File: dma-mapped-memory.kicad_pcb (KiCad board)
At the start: 4 copper layers, 99.8 x 99.8 mm, 27 parts, among them J1 Conn_01x02_Male, J2 Conn_01x02_Male, J3 Conn_02x30_Odd_Even, U1 AS6C8008-55, U10 74LS157, U11 74LS157, U12 74LS157, U13 74LS157, U14 74LS157, U15 74LS04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

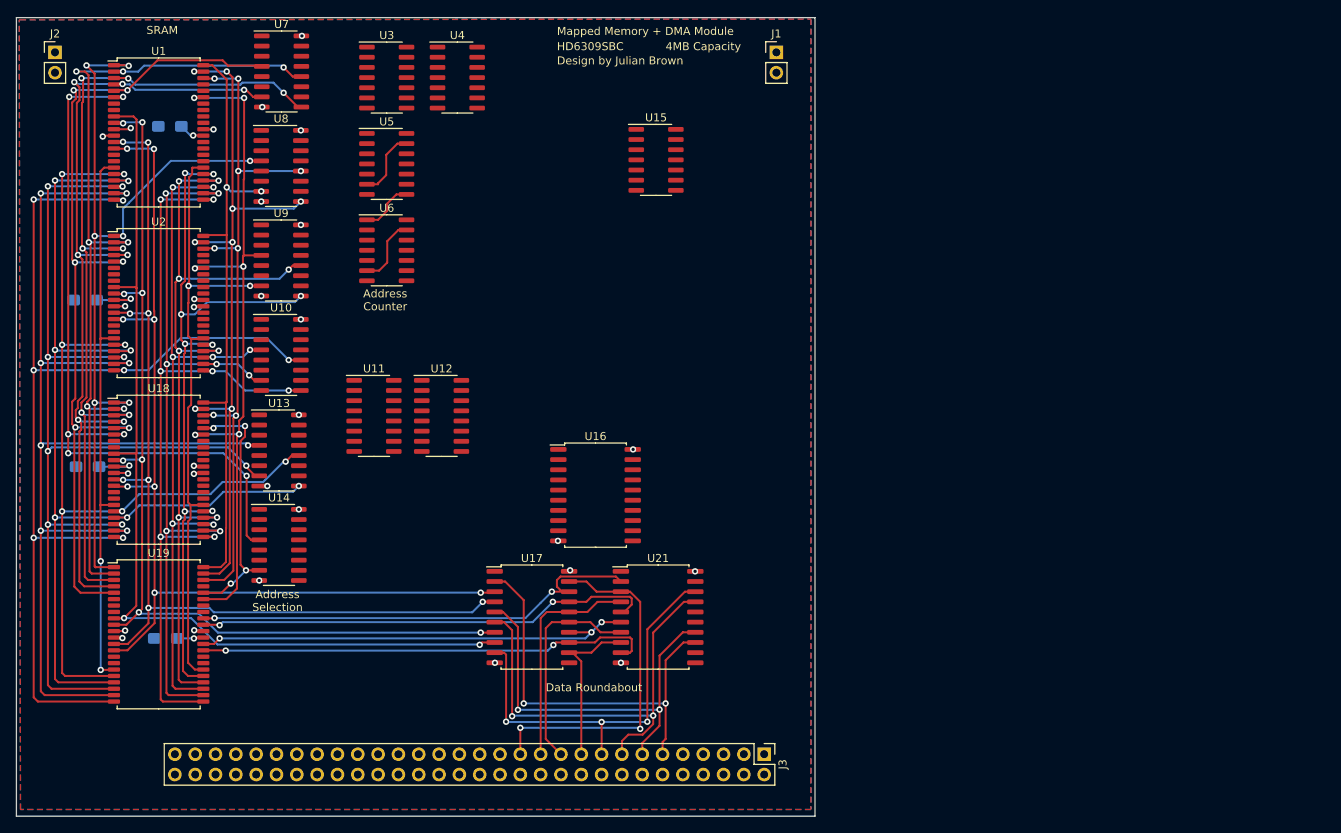
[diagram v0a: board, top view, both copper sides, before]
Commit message: add address registers
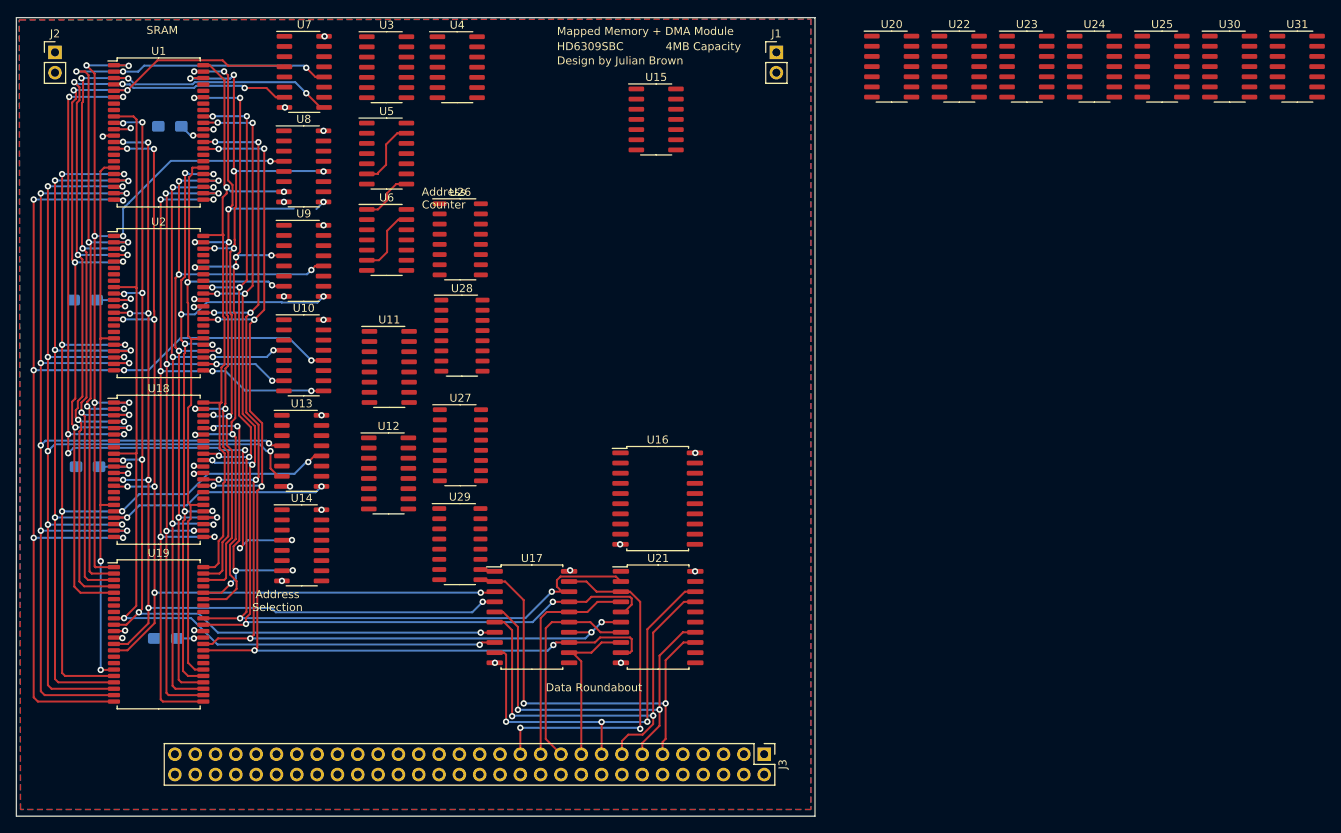
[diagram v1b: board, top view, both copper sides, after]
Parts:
- added U20: 74HC08, Package_SO:SO-14_3.9x8.65mm_P1.27mm, F.Cu at (206.6, 50.3)
- added U22: 74HC21, Package_SO:SO-14_3.9x8.65mm_P1.27mm, F.Cu at (215.0, 50.3)
- added U23: 74HC02, Package_SO:SO-14_3.9x8.65mm_P1.27mm, F.Cu at (223.5, 50.3)
- added U24: 74HC21, Package_SO:SO-14_3.9x8.65mm_P1.27mm, F.Cu at (231.9, 50.3)
- added U25: 74HC04, Package_SO:SO-14_3.9x8.65mm_P1.27mm, F.Cu at (240.4, 50.3)
- added U26: 74HC375, Package_SO:SO-16_3.9x9.9mm_P1.27mm, F.Cu at (152.6, 71.9)
- added U27: 74HC375, Package_SO:SO-16_3.9x9.9mm_P1.27mm, F.Cu at (152.7, 97.6)
- added U28: 74HC375, Package_SO:SO-16_3.9x9.9mm_P1.27mm, F.Cu at (152.8, 83.9)
- added U29: 74HC375, Package_SO:SO-16_3.9x9.9mm_P1.27mm, F.Cu at (152.6, 110.0)
- added U30: 74HC21, Package_SO:SO-14_3.9x8.65mm_P1.27mm, F.Cu at (248.8, 50.3)
- added U31: 74HC04, Package_SO:SO-14_3.9x8.65mm_P1.27mm, F.Cu at (257.3, 50.3)
- moved U12 9.78 mm to (143.7, 101.2)
- moved U16 7.78 mm to (177.3, 104.3)
- moved U11 6.41 mm to (143.8, 87.9)
- moved U15 5.05 mm to (177.1, 56.9)
- moved U10 2.83 mm to (133.1, 86.4)
- moved U7 2.83 mm to (133.1, 51.0)
- moved U8 2.83 mm to (133.1, 62.8)
- moved U13 2.83 mm to (132.8, 98.3)
- moved U14 2.83 mm to (132.8, 110.2)
- moved U9 2.83 mm to (133.1, 74.6)
- moved U3 1.30 mm to (143.4, 50.4)
- moved U4 1.30 mm to (152.3, 50.4)
- moved U5 1.30 mm to (143.4, 61.2)
- moved U6 1.30 mm to (143.4, 72.0)
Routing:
- net DQ4: track 57.2 -> 143.2 mm, vias 2 -> 8
- net DQ5: track 56.2 -> 139.2 mm, vias 3 -> 9
- net DQ6: track 57.7 -> 139.6 mm, vias 2 -> 8
- net DQ7: track 58.2 -> 138.4 mm, vias 2 -> 8
- net DA20: track 94.1 -> 104.4 mm, vias 6 -> 8
- net DA7: track 86.7 -> 92.9 mm
- net DA21: track 32.0 -> 37.2 mm, vias 4 -> 5
- net DA17: track 130.6 -> 135.4 mm
- net DA9: track 78.5 -> 81.9 mm
- net DA3: track 110.1 -> 113.3 mm
- net DA16: track 136.9 -> 140.0 mm
- net DA1: track 108.7 -> 111.8 mm
- net DA0: track 111.3 -> 114.3 mm
- net DA10: track 95.7 -> 98.5 mm
- net DA2: track 112.1 -> 115.0 mm
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
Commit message: simplify logic
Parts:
- removed U25, U31: 74HC04, Package_SO:SO-14_3.9x8.65mm_P1.27mm
- moved U16 11.2 mm to (188.2, 101.4)
- moved U17 11.2 mm to (172.4, 116.2)
- moved U21 11.2 mm to (188.2, 116.2)
- moved U11 4.14 mm to (143.9, 83.7)
- moved U26 3.79 mm to (152.7, 75.7)
- moved U28 3.76 mm to (152.7, 87.7)
- moved U27 1.81 mm to (152.9, 99.5)
- moved U12 1.81 mm to (143.9, 103.0)
- moved U29 1.30 mm to (152.8, 111.3)
- moved U3 0.45 mm to (143.9, 50.3)
- moved U4 0.45 mm to (152.7, 50.3)
- moved U5 0.45 mm to (143.9, 61.1)
- moved U6 0.45 mm to (143.9, 71.9)
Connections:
- U1 pad 40: Net-(U1-CE2) -> ~{DA21}
- U1 pad 41: unconnected-(U1-~{OE}-Pad41) -> E
- U15 pad 10: Net-(U17-OE) -> ~{R}/W
- U15 pad 12: Net-(U21-LE) -> unconnected-(U15-Pad12)
- U15 pad 13: R/~{W} -> unconnected-(U15-Pad13)
- U15 pad 2: Net-(U2-~{CE}) -> ~{DA20}
- U15 pad 3: DA21 -> unconnected-(U15-Pad3)
- U15 pad 4: Net-(U1-CE2) -> unconnected-(U15-Pad4)
- U15 pad 6: Net-(U2-CE2) -> ~{DA21}
- U15 pad 8: Net-(U19-~{CE}) -> unconnected-(U15-Pad8)
- U15 pad 9: DA20 -> unconnected-(U15-Pad9)
- U17 pad 1: Net-(U17-OE) -> ~{R}/W
- U18 pad 41: unconnected-(U18-~{OE}-Pad41) -> E
- U19 pad 41: unconnected-(U19-~{OE}-Pad41) -> E
- U19 pad 6: Net-(U19-~{CE}) -> ~{DA20}
- U2 pad 40: Net-(U2-CE2) -> ~{DA21}
- U2 pad 41: unconnected-(U2-~{OE}-Pad41) -> E
- U2 pad 6: Net-(U2-~{CE}) -> ~{DA20}
- U21 pad 11: Net-(U21-LE) -> ~{R}/W
- U24 pad 9: Net-(U24-Pad9) -> ~{R}/W
- U28 pad 1: D0 -> D1
- U28 pad 3: PBA0 -> PBA1
- U28 pad 5: PBA1 -> PBA0
- U28 pad 7: D1 -> D0
- U29 pad 1: D4 -> D5
- U29 pad 3: PBA4 -> PBA5
- U29 pad 5: PBA5 -> PBA4
- U29 pad 7: D5 -> D4
- U30 pad 9: Net-(U30-Pad9) -> ~{R}/W
- U6 pad 13: Net-(U6A-Q3) -> AM10
- U6 pad 6: Net-(U6A-Q3) -> AM10
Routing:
- net E: track 0.00 -> 267.6 mm, vias 0 -> 9
- net DQ5: track 139.2 -> 95.6 mm
- net D2: track 55.7 -> 12.2 mm, vias 2 -> 0
- net DQ0: track 123.6 -> 82.8 mm, vias 8 -> 7
- net D0: track 51.8 -> 11.3 mm, vias 2 -> 0
- net DQ4: track 143.2 -> 103.7 mm
- net D3: track 51.1 -> 13.5 mm, vias 3 -> 0
- net DQ6: track 139.6 -> 102.7 mm
- net D1: track 50.7 -> 13.8 mm, vias 2 -> 0
- net DQ7: track 138.4 -> 102.2 mm
- net DQ2: track 121.6 -> 88.7 mm
- net DQ3: track 120.8 -> 88.0 mm
- net AM17: track 0.00 -> 31.2 mm, vias 0 -> 2
- net D7: track 44.2 -> 13.2 mm, vias 2 -> 0
- net AM13: track 0.00 -> 28.8 mm, vias 0 -> 4
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
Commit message: continue hand tracing
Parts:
- moved U15 84.7 mm to (132.5, 128.9)
- moved U30 81.1 mm to (178.1, 90.0)
- moved U22 67.7 mm to (169.7, 100.6)
- moved U23 66.9 mm to (169.7, 90.0)
- moved U24 61.3 mm to (178.0, 79.5)
- moved U20 41.5 mm to (169.9, 69.7)
- moved U17 2.19 mm to (174.6, 116.2)
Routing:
- net ~{DA21}: track 0.00 -> 91.1 mm, vias 0 -> 2
- net A0: track 4.94 -> 95.6 mm
- net A3: track 5.35 -> 91.5 mm
- net A1: track 5.13 -> 89.2 mm
- net A2: track 4.79 -> 88.4 mm
- net A5: track 5.21 -> 87.3 mm
- net ~{DA20}: track 0.00 -> 80.2 mm, vias 0 -> 2
- net A4: track 5.29 -> 79.3 mm
- net A7: track 4.66 -> 78.1 mm
- net A11: track 5.22 -> 78.3 mm, vias 0 -> 2
- net A12: track 5.21 -> 76.6 mm, vias 0 -> 2
- net A8: track 5.33 -> 74.5 mm, vias 0 -> 2
- net A13: track 5.42 -> 74.4 mm, vias 0 -> 2
- net A6: track 5.27 -> 73.8 mm
- net A10: track 5.25 -> 73.3 mm, vias 0 -> 2
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
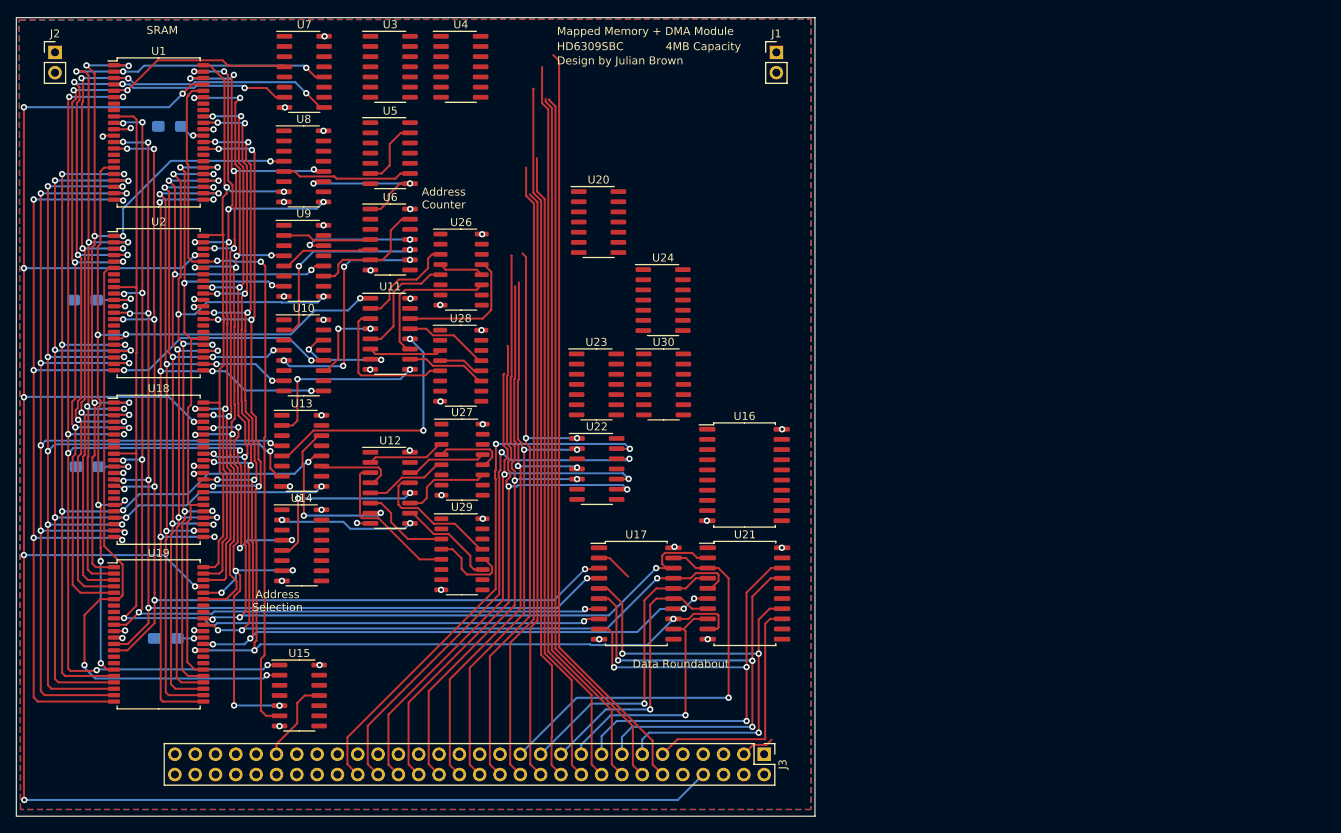
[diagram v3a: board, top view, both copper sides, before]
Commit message: add addressing
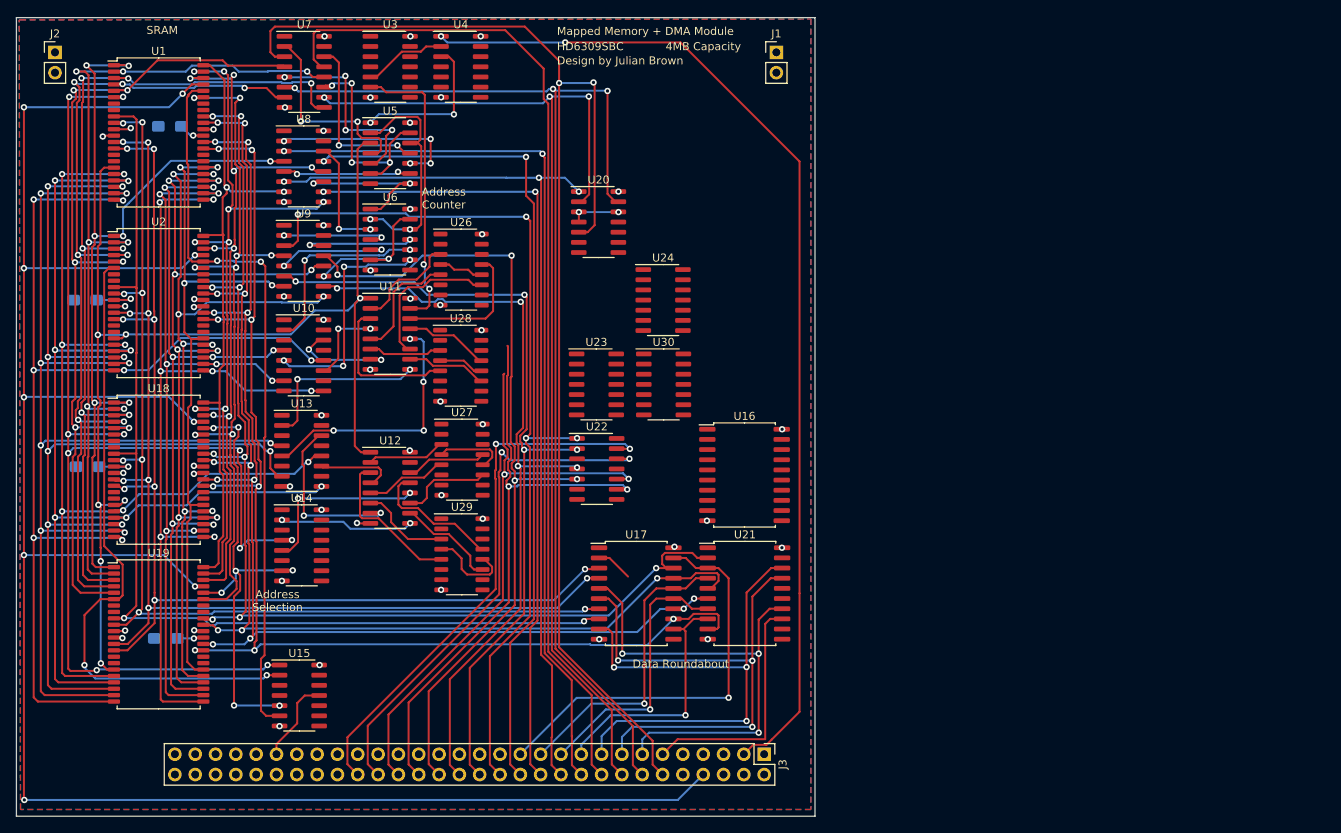
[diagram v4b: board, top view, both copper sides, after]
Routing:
- net Clock24: track 4.24 -> 129.2 mm, vias 0 -> 2
- net A0: track 95.6 -> 161.9 mm, vias 0 -> 2
- net A1: track 89.2 -> 145.8 mm, vias 0 -> 3
- net A2: track 88.4 -> 136.1 mm, vias 0 -> 3
- net DMR/~{DMW}: track 108.7 -> 150.4 mm
- net A8: track 74.5 -> 113.4 mm, vias 2 -> 4
- net ~{DMA_RUN}: track 0.00 -> 36.5 mm, vias 0 -> 2
- net A3: track 91.5 -> 127.1 mm
- net A4: track 79.3 -> 112.1 mm, vias 0 -> 2
- net A9: track 72.0 -> 101.7 mm, vias 2 -> 4
- net CR: track 0.00 -> 29.7 mm, vias 0 -> 2
- net A7: track 78.1 -> 104.9 mm, vias 0 -> 2
- net A6: track 73.8 -> 100.4 mm, vias 0 -> 2
- net A5: track 87.3 -> 113.6 mm, vias 0 -> 3
- net A11: track 78.3 -> 104.5 mm, vias 2 -> 4
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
